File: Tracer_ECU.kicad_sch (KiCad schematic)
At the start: 166 parts, among them IC1 R5F572TFADFP#30, IC2 MPU-6500, IC3 DRV8320HRTVR, IC4 DRV8320HRTVR, IC5 DRV8320HRTVR, J1 BAT, J10 ENC2, J11 SENS2, J13 SDC, J14 ENC3, J2 DBG, J3 SENS1, J4 MOT3, J5 MOT1, J6 LIGHIT, J8 MOT2, J9 ENC1, Q1 TJ60S04M3L, Q10 FDS6898A, Q11 FDS6898A, Q12 FDS6898A, Q2 FDS6898A, Q3 FDS6898A, Q4 FDS6898A, Q6 IRLML6344TRPBF, Q7 FDS6898A, Q8 FDS6898A, Q9 FDS6898A, SW1 SW_SPDT, SW2 SW_Push, SW4 SW_Push, SW5 SW_Push, U1 NJM2732, U2 AZ1117-3.3, Y1 CSTNE20M

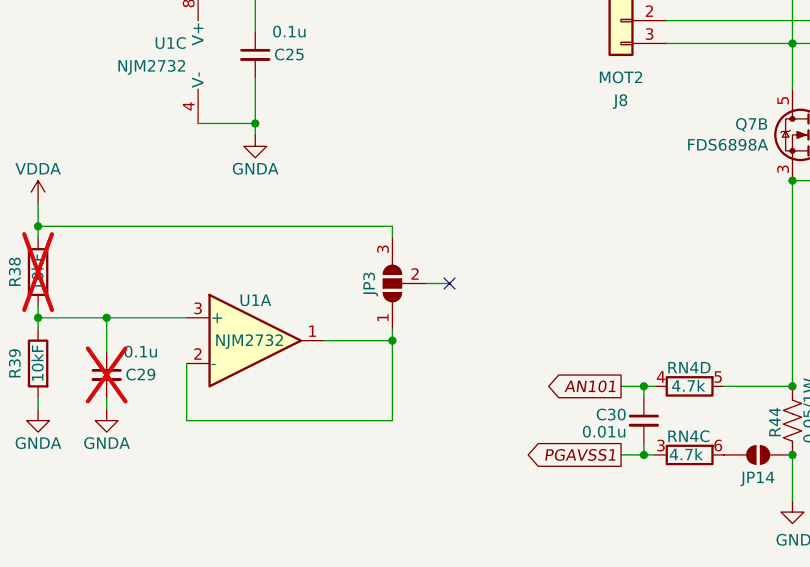
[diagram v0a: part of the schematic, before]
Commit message: PCB配線完了.(未配線ゼロ)
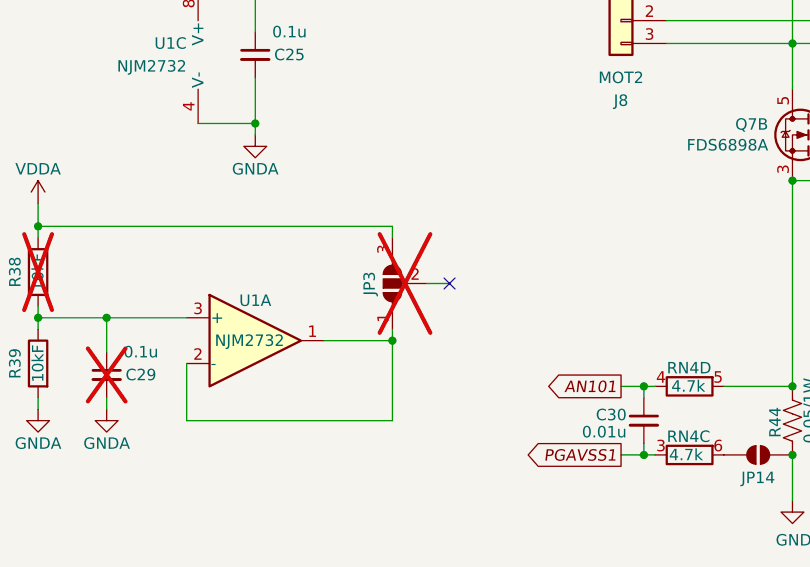
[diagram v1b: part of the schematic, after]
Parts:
- JP3: now not fitted
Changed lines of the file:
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@@
 		(exclude_from_sim no)
 		(in_bom yes)
-		(on_board yes)
-		(dnp no)
+		(on_board no)
+		(dnp yes)
 		(property "Reference" "JP3"
 			(at 344.17 231.14 0)

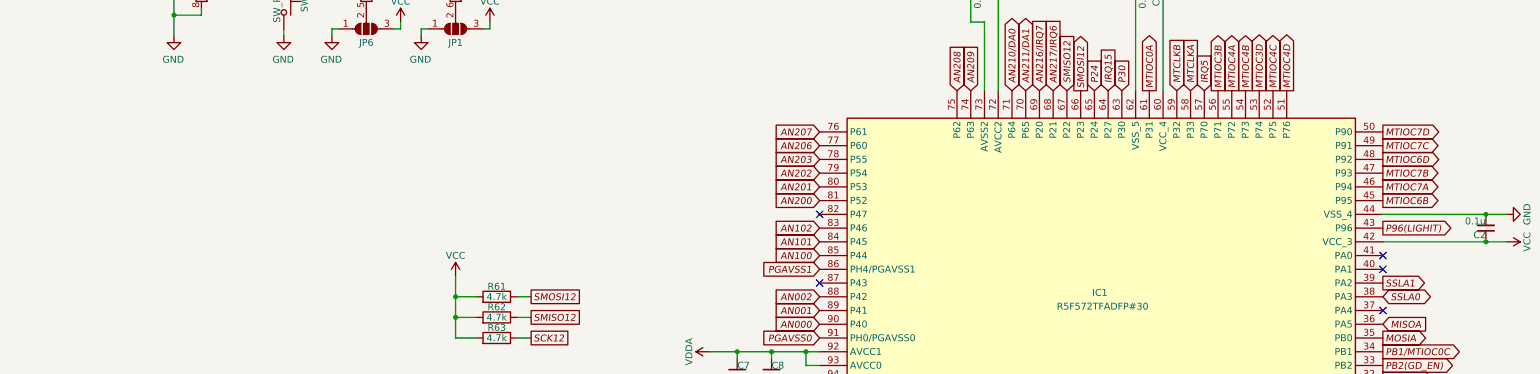
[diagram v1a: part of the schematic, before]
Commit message: LCD用ポートコネクタを追加．(I2C端子)
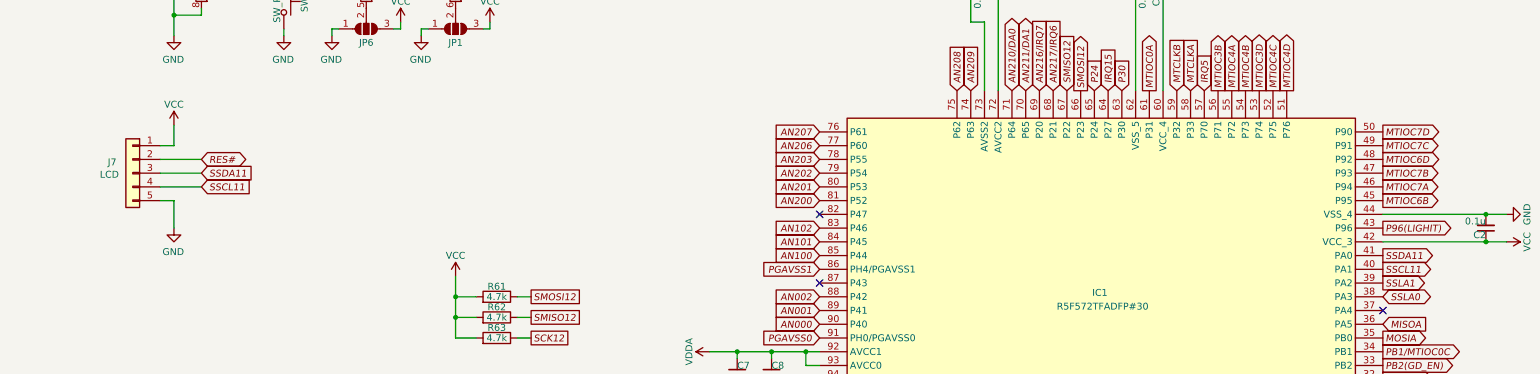
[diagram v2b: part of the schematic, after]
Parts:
- added J7: LCD, Connector_Molex:Molex_PicoBlade_53047-0510_1x05_P1.25mm_Vertical, symbol Connector_Generic:Conn_01x05
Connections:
- net GND: now also J7.5 (Pin_5)
- net RES#: now also J7.2 (Pin_2)
- net VCC: now also J7.1 (Pin_1)
- net SSCL11: now reaches IC1.40 (PA1)
- net SSCL11: now also J7.4 (Pin_4)
- net SSDA11: now reaches IC1.41 (PA0)
- net SSDA11: now also J7.3 (Pin_3)
- no-connect marks 12 -> 10

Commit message: 電流センス回路フィルタ用集合Ｒ変更　4.7k → 470
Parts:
- RN3, RN4, RN5: value 4.7k -> 470
